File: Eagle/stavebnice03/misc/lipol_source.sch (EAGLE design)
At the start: 24 parts

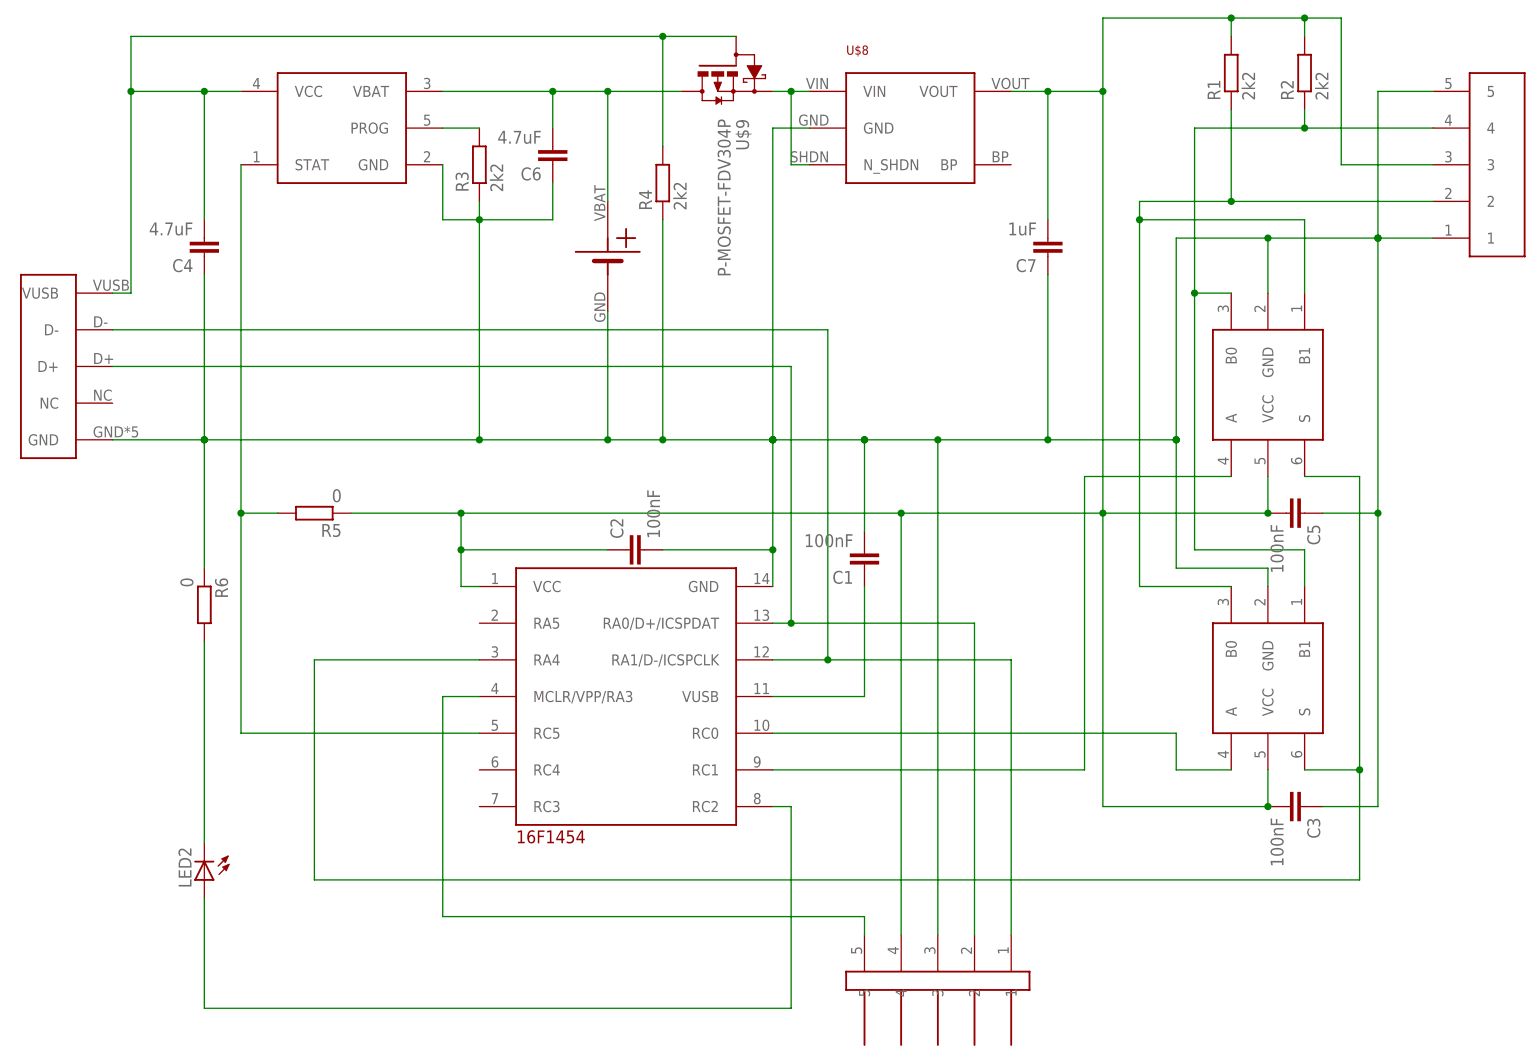
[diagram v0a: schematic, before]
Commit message: values for lipol charger
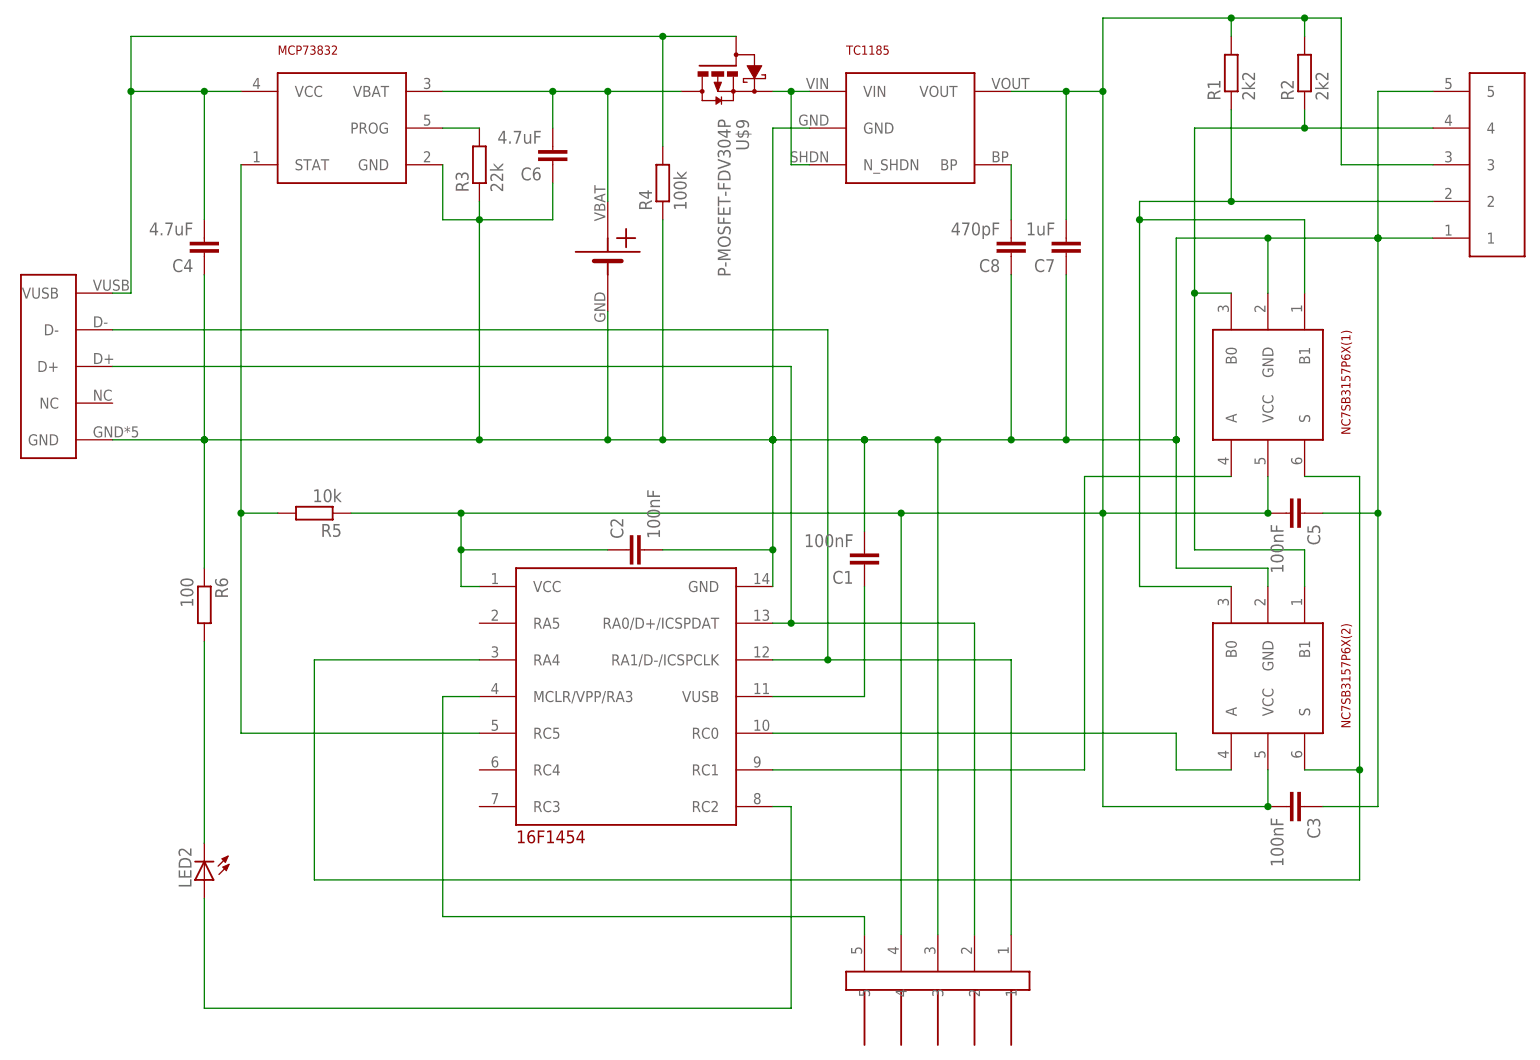
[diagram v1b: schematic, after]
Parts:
- added C8: 470pF, resistor:C-EUC0603
- R3: value 2k2 -> 22k
- R4: value 2k2 -> 100k
- R5: value 0 -> 10k
- R6: value 0 -> 100
- renumbered U$4 to MCP73832, U$6 to NC7SB3157P6X(1), U$7 to NC7SB3157P6X(2), U$8 to TC1185
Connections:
- new net N$17: C8.2, TC1185.BP
- net GND: now also C8.1
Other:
- moved on the sheet: C7

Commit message: LED resistor increased to a size 0805
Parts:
- R6: device resistor:R-EU_R0603 -> resistor:R-EU_R0805
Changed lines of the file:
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@@
 <part name="U$10" library="!stavebnice03" deviceset="JUMPER5M-90" device=""/>
 <part name="R5" library="resistor" deviceset="R-EU_" device="R0603" value="10k"/>
-<part name="R6" library="resistor" deviceset="R-EU_" device="R0603" value="100"/>
+<part name="R6" library="resistor" deviceset="R-EU_" device="R0805" value="100"/>
 <part name="LED2" library="led" deviceset="LED" device="3MM"/>
 <part name="C8" library="resistor" deviceset="C-EU" device="C0603" value="470pF"/>

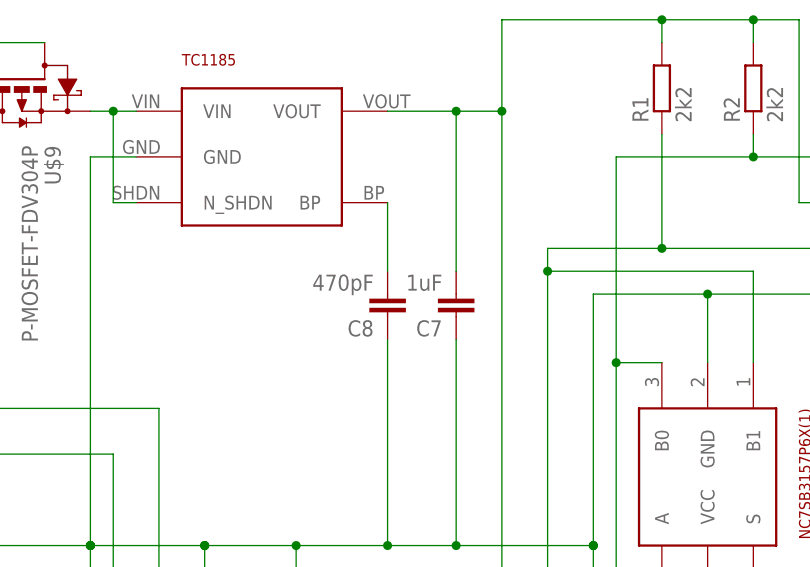
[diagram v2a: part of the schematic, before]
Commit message: adjutet elemet values
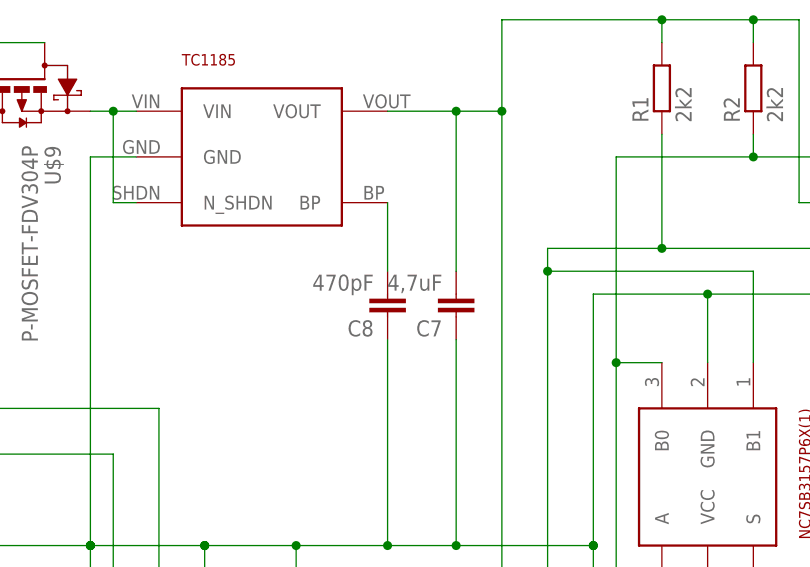
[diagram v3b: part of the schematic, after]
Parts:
- C7: value 1uF -> 4,7uF
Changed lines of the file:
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@@
 <part name="U$9" library="!stavebnice03" deviceset="P-MOSFET-FDV304P" device=""/>
 <part name="R4" library="resistor" deviceset="R-EU_" device="R0603" value="100k"/>
-<part name="C7" library="resistor" deviceset="C-EU" device="C0603" value="1uF"/>
+<part name="C7" library="resistor" deviceset="C-EU" device="C0603" value="4,7uF"/>
 <part name="U$10" library="!stavebnice03" deviceset="JUMPER5M-90" device=""/>
 <part name="R5" library="resistor" deviceset="R-EU_" device="R0603" value="10k"/>

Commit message: added pin and resistor to stay in bootloader + changed size back to 21x21 mm
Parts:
- R6: device resistor:R-EU_R0805 -> resistor:R-EU_R0603
- U$10: value JUMPER5M-90 -> JUMPER5M; device !stavebnice03:JUMPER5M-90 -> !stavebnice03:JUMPER5M
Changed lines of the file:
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@@
 <part name="R4" library="resistor" deviceset="R-EU_" device="R0603" value="100k"/>
 <part name="C7" library="resistor" deviceset="C-EU" device="C0603" value="4,7uF"/>
-<part name="U$10" library="!stavebnice03" deviceset="JUMPER5M-90" device=""/>
+<part name="U$10" library="!stavebnice03" deviceset="JUMPER5M" device=""/>
 <part name="R5" library="resistor" deviceset="R-EU_" device="R0603" value="10k"/>
-<part name="R6" library="resistor" deviceset="R-EU_" device="R0805" value="100"/>
+<part name="R6" library="resistor" deviceset="R-EU_" device="R0603" value="100"/>
 <part name="LED2" library="led" deviceset="LED" device="3MM"/>
 <part name="C8" library="resistor" deviceset="C-EU" device="C0603" value="470pF"/>

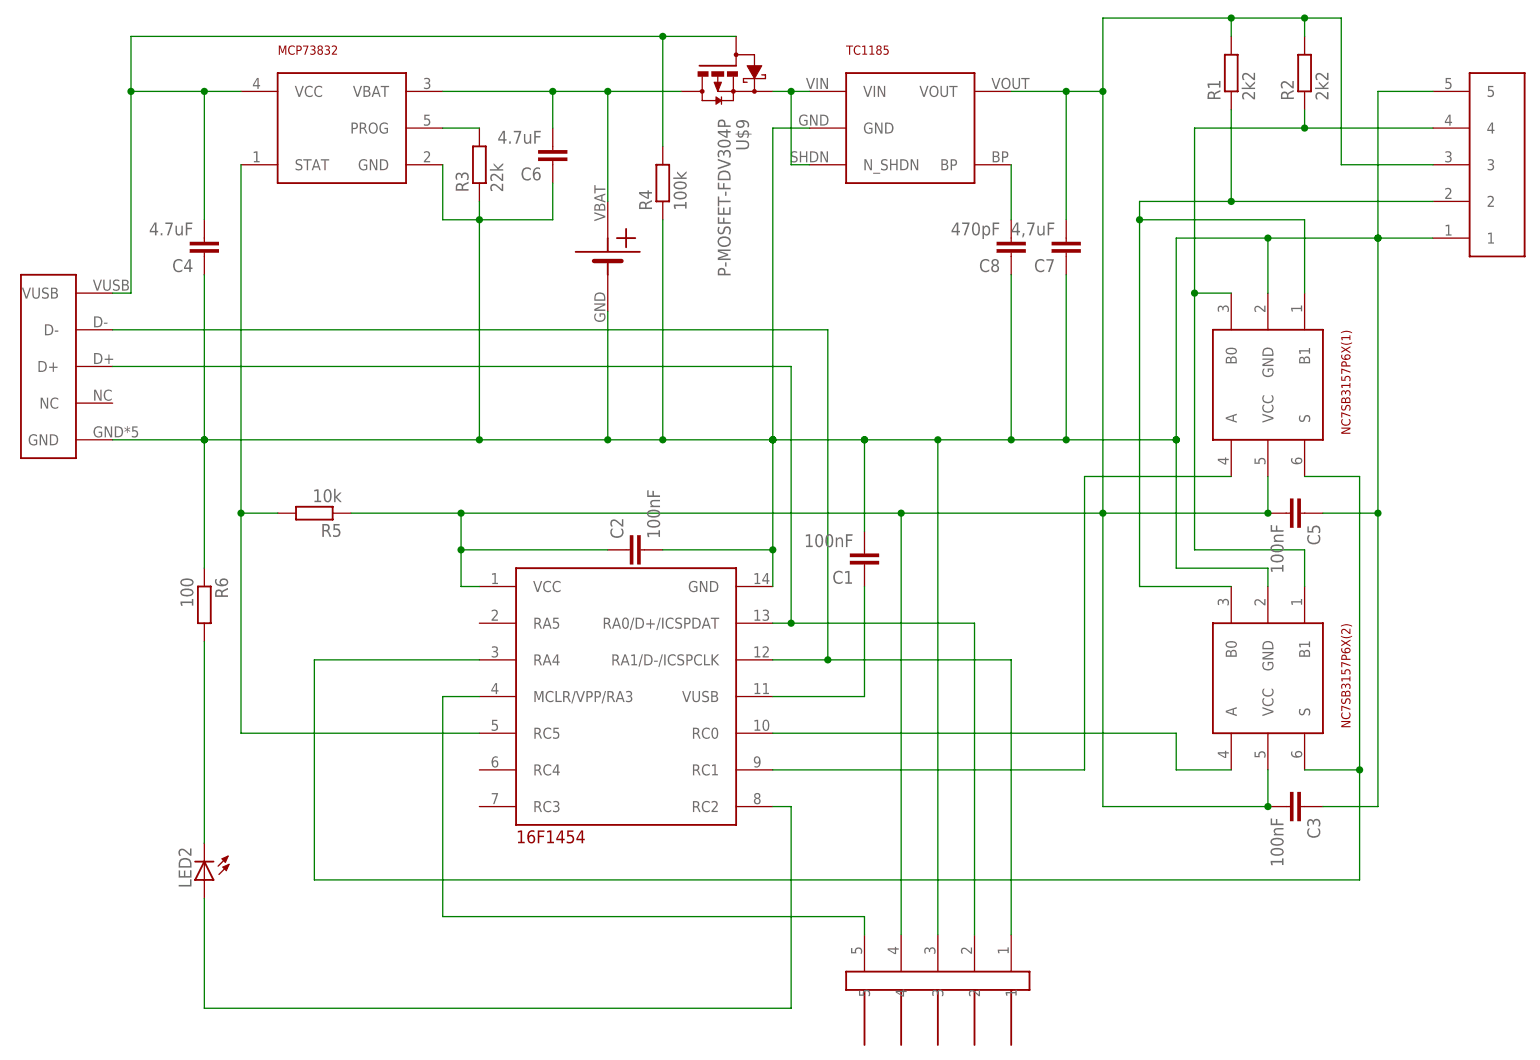
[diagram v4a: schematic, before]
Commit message: fix of bugs on rgb and lipol board + a few minor changes
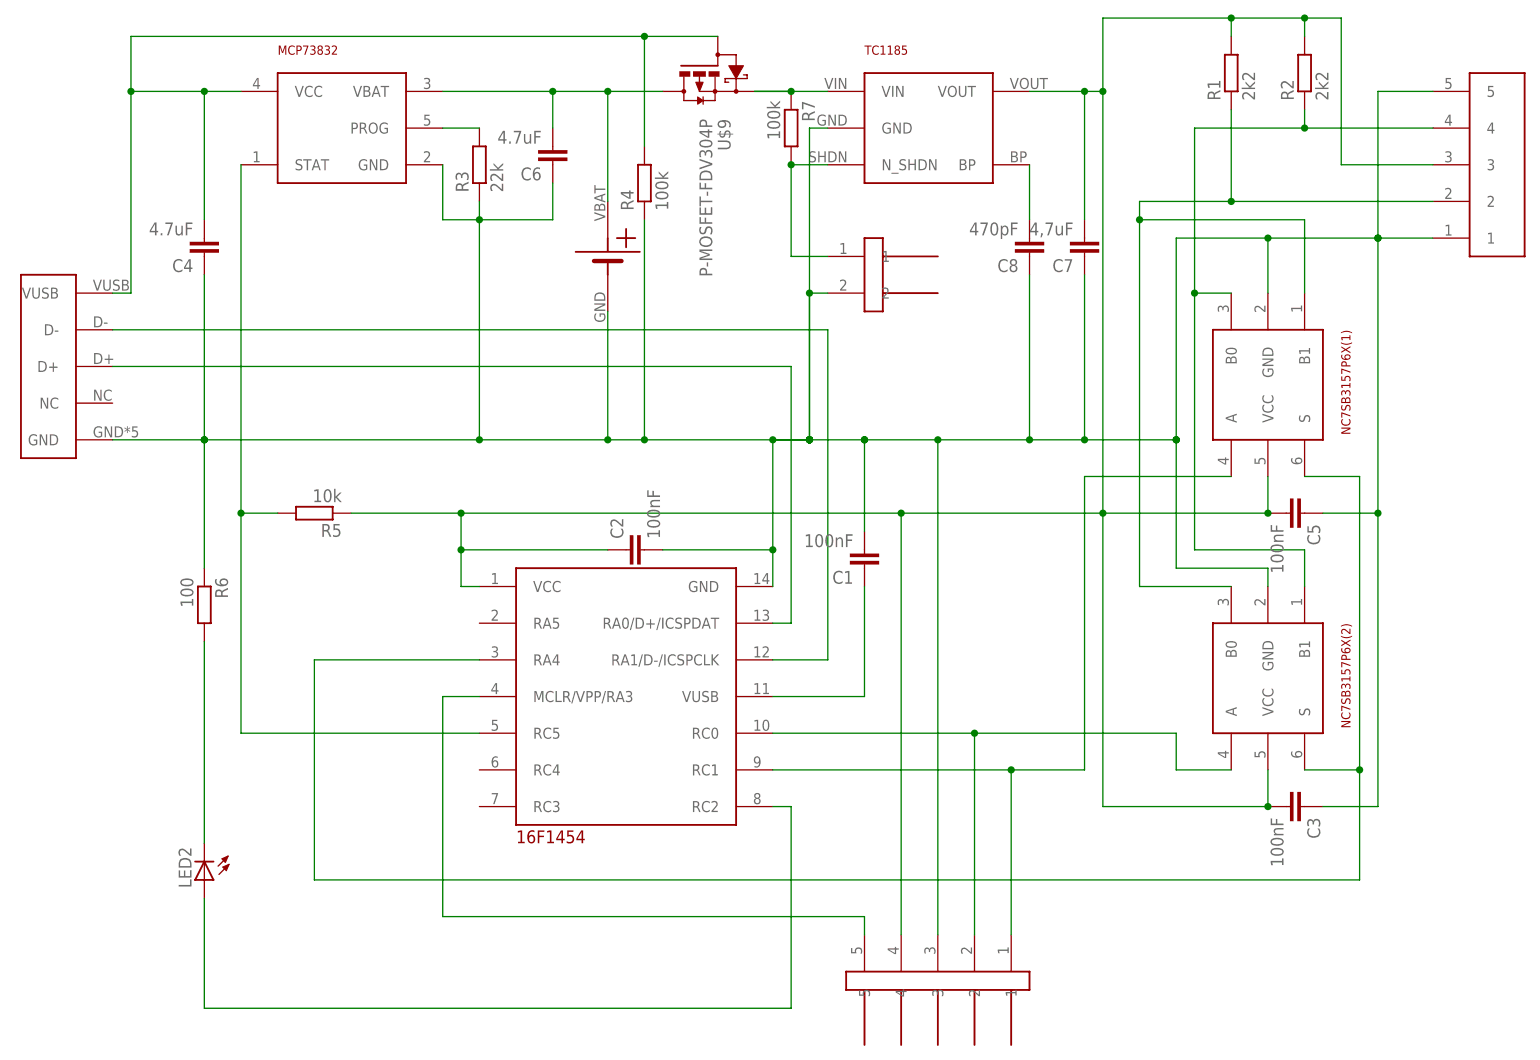
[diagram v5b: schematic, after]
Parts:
- added R7: 100k, resistor:R-EU_R0603
- added U$4: JUMPER2M, !stavebnice03:JUMPER2M
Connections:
- new net N$20: R7.2, TC1185.N_SHDN, U$4.1
- net GND: now also U$4.2
- net N$12: now also R7.1; no longer TC1185.N_SHDN
- net N$2: no longer U$10.1
- net N$4: now also U$10.2
- net N$5: no longer U$10.2
- net N$7: now also U$10.1
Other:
- moved on the sheet: C7, C8, R4, TC1185, U$9

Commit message: C0603 changed to C0603K with wider space between soldering areas
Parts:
- C1, C2, C3, C4, C5, C6, C7, C8: device resistor:C-EUC0603 -> resistor:C-EUC0603K
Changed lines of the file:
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@@
 <parts>
 <part name="U$1" library="!stavebnice03" deviceset="16F1454" device=""/>
-<part name="C2" library="resistor" deviceset="C-EU" device="C0603" value="100nF"/>
+<part name="C2" library="resistor" deviceset="C-EU" device="C0603K" value="100nF"/>
 <part name="R1" library="resistor" deviceset="R-EU_" device="R0603" value="2k2"/>
 <part name="R2" library="resistor" deviceset="R-EU_" device="R0603" value="2k2"/>
-<part name="C3" library="resistor" deviceset="C-EU" device="C0603" value="100nF"/>
+<part name="C3" library="resistor" deviceset="C-EU" device="C0603K" value="100nF"/>
 <part name="U$5" library="!stavebnice03" deviceset="JUMPER5F-90" device=""/>
 <part name="NC7SB3157P6X(1)" library="!stavebnice03" deviceset="NC7SB3157P6X" device=""/>
 <part name="NC7SB3157P6X(2)" library="!stavebnice03" deviceset="NC7SB3157P6X" device=""/>
-<part name="C5" library="resistor" deviceset="C-EU" device="C0603" value="100nF"/>
+<part name="C5" library="resistor" deviceset="C-EU" device="C0603K" value="100nF"/>
 <part name="U$2" library="!stavebnice03" deviceset="USBMICRO" device=""/>
-<part name="C1" library="resistor" deviceset="C-EU" device="C0603" value="100nF"/>
+<part name="C1" library="resistor" deviceset="C-EU" device="C0603K" value="100nF"/>
 <part name="U$3" library="!stavebnice03" deviceset="LIPOL_21X17" device=""/>
 <part name="MCP73832" library="!stavebnice03" deviceset="MCP73831" device=""/>
 <part name="R3" library="resistor" deviceset="R-EU_" device="R0603" value="22k"/>
-<part name="C4" library="resistor" deviceset="C-EU" device="C0603" value="4.7uF"/>
-<part name="C6" library="resistor" deviceset="C-EU" device="C0603" value="4.7uF"/>
+<part name="C4" library="resistor" deviceset="C-EU" device="C0603K" value="4.7uF"/>
+<part name="C6" library="resistor" deviceset="C-EU" device="C0603K" value="4.7uF"/>
 <part name="TC1185" library="!stavebnice03" deviceset="STABILISER_APE8865" device=""/>
 <part name="U$9" library="!stavebnice03" deviceset="P-MOSFET-FDV304P" device=""/>
 <part name="R4" library="resistor" deviceset="R-EU_" device="R0603" value="100k"/>
-<part name="C7" library="resistor" deviceset="C-EU" device="C0603" value="4,7uF"/>
+<part name="C7" library="resistor" deviceset="C-EU" device="C0603K" value="4,7uF"/>
 <part name="U$10" library="!stavebnice03" deviceset="JUMPER5M" device=""/>
 <part name="R5" library="resistor" deviceset="R-EU_" device="R0603" value="10k"/>
 <part name="R6" library="resistor" deviceset="R-EU_" device="R0603" value="100"/>
 <part name="LED2" library="led" deviceset="LED" device="3MM"/>
-<part name="C8" library="resistor" deviceset="C-EU" device="C0603" value="470pF"/>
+<part name="C8" library="resistor" deviceset="C-EU" device="C0603K" value="470pF"/>
 <part name="R7" library="resistor" deviceset="R-EU_" device="R0603" value="100k"/>
 <part name="U$4" library="!stavebnice03" deviceset="JUMPER2M" device=""/>
